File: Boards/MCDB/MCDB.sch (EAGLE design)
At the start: 61 parts, among them IC1 MC33926

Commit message: continued work on MCDB
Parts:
- added C25: 22 pF, pie:CAP0603-CAP
- added C26: 22pF, pie:CAP0603-CAP
- added C27: .1 uF, pie:CAP0603-CAP
- added C28: 1 uF, pie:CAP0603-CAP
- added R4: >VALUE, pie:R-US_R0603
- added Y1: 16MHz, pie:CRYSTAL7.6X4.1
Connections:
- new net N$17: C25.2, U$1.XTAL1, Y1.2
- new net N$18: C26.2, U$1.XTAL2, Y1.1
- new net N$19: C27.2, U$1.AREF
- new net N$21: R4.1, U$1.!RESET
- net GND: now also C25.1, C26.1, C27.1, C28.1
- net VCC: now also C28.2, R4.2
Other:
- moved on the sheet: UCAP
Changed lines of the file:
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@@
 <part name="UCAP" library="pie" deviceset="CAP" device="0603-CAP" value="1 uF"/>
 <part name="SUPPLY15" library="pie" deviceset="GND" device=""/>
+<part name="Y1" library="pie" deviceset="CRYSTAL" device="7.6X4.1" value="16MHz"/>
+<part name="C25" library="pie" deviceset="CAP" device="0603-CAP" value="22 pF"/>
+<part name="C26" library="pie" deviceset="CAP" device="0603-CAP" value="22pF"/>
+<part name="SUPPLY16" library="pie" deviceset="GND" device=""/>
+<part name="SUPPLY21" library="pie" deviceset="GND" device=""/>
+<part name="C27" library="pie" deviceset="CAP" device="0603-CAP" value=".1 uF"/>
+<part name="SUPPLY22" library="pie" deviceset="GND" device=""/>
+<part name="C28" library="pie" deviceset="CAP" device="0603-CAP" value="1 uF"/>
+<part name="SUPPLY23" library="pie" deviceset="GND" device=""/>
+<part name="R4" library="pie" deviceset="R-US_" device="R0603" value="&gt;VALUE"/>
 </parts>
 <sheets>
@@
 <attribute name="VALUE" x="157.48" y="78.74" size="1.778" layer="96"/>
 </instance>
-<instance part="UCAP" gate="G$1" x="134.62" y="121.92" smashed="yes" rot="R90">
-<attribute name="NAME" x="132.08" y="118.11" size="1.778" layer="95" rot="R90"/>
-<attribute name="VALUE" x="139.7" y="118.11" size="1.778" layer="96" rot="R90"/>
-</instance>
-<instance part="SUPPLY15" gate="GND" x="134.62" y="111.76" smashed="yes">
-<attribute name="VALUE" x="133.35" y="107.95" size="1.778" layer="96"/>
+<instance part="UCAP" gate="G$1" x="114.3" y="121.92" smashed="yes" rot="R90">
+<attribute name="NAME" x="111.76" y="118.11" size="1.778" layer="95" rot="R90"/>
+<attribute name="VALUE" x="119.38" y="118.11" size="1.778" layer="96" rot="R90"/>
+</instance>
+<instance part="SUPPLY15" gate="GND" x="114.3" y="111.76" smashed="yes">
+<attribute name="VALUE" x="113.03" y="107.95" size="1.778" layer="96"/>
+</instance>
+<instance part="Y1" gate="G$1" x="147.32" y="109.22" smashed="yes" rot="R90">
+<attribute name="NAME" x="144.78" y="109.22" size="1.778" layer="95" rot="R90"/>
+<attribute name="VALUE" x="151.13" y="106.68" size="1.778" layer="96" rot="R90"/>
+</instance>
+<instance part="C25" gate="G$1" x="129.54" y="111.76" smashed="yes">
+<attribute name="NAME" x="125.73" y="114.3" size="1.778" layer="95"/>
+<attribute name="VALUE" x="125.73" y="106.68" size="1.778" layer="96"/>
+</instance>
+<instance part="C26" gate="G$1" x="139.7" y="106.68" smashed="yes">
+<attribute name="NAME" x="135.89" y="109.22" size="1.778" layer="95"/>
+<attribute name="VALUE" x="135.89" y="101.6" size="1.778" layer="96"/>
+</instance>
+<instance part="SUPPLY16" gate="GND" x="124.46" y="104.14" smashed="yes">
+<attribute name="VALUE" x="123.19" y="100.33" size="1.778" layer="96"/>
+</instance>
+<instance part="SUPPLY21" gate="GND" x="134.62" y="99.06" smashed="yes">
+<attribute name="VALUE" x="133.35" y="95.25" size="1.778" layer="96"/>
+</instance>
+<instance part="C27" gate="G$1" x="142.24" y="139.7" smashed="yes" rot="R90">
+<attribute name="NAME" x="139.7" y="135.89" size="1.778" layer="95" rot="R90"/>
+<attribute name="VALUE" x="147.32" y="135.89" size="1.778" layer="96" rot="R90"/>
+</instance>
+<instance part="SUPPLY22" gate="GND" x="142.24" y="132.08" smashed="yes">
+<attribute name="VALUE" x="140.97" y="128.27" size="1.778" layer="96"/>
+</instance>
+<instance part="C28" gate="G$1" x="121.92" y="139.7" smashed="yes" rot="R90">
+<attribute name="NAME" x="119.38" y="135.89" size="1.778" layer="95" rot="R90"/>
+<attribute name="VALUE" x="127" y="135.89" size="1.778" layer="96" rot="R90"/>
+</instance>
+<instance part="SUPPLY23" gate="GND" x="121.92" y="132.08" smashed="yes">
+<attribute name="VALUE" x="120.65" y="128.27" size="1.778" layer="96"/>
+</instance>
+<instance part="R4" gate="G$1" x="152.4" y="167.64" smashed="yes" rot="R90">
+<attribute name="NAME" x="149.86" y="162.56" size="1.778" layer="95" rot="R90"/>
+<attribute name="VALUE" x="156.21" y="162.56" size="1.778" layer="96" rot="R90"/>
 </instance>
 </instances>
@@
 <pinref part="SUPPLY15" gate="GND" pin="GND"/>
 <pinref part="UCAP" gate="G$1" pin="1"/>
-<wire x1="134.62" y1="114.3" x2="134.62" y2="119.38" width="0.1524" layer="91"/>
+<wire x1="114.3" y1="114.3" x2="114.3" y2="119.38" width="0.1524" layer="91"/>
+</segment>
+<segment>
+<pinref part="C25" gate="G$1" pin="1"/>
+<pinref part="SUPPLY16" gate="GND" pin="GND"/>
+<wire x1="127" y1="111.76" x2="124.46" y2="111.76" width="0.1524" layer="91"/>
+<wire x1="124.46" y1="111.76" x2="124.46" y2="106.68" width="0.1524" layer="91"/>
+</segment>
+<segment>
+<pinref part="C26" gate="G$1" pin="1"/>
+<pinref part="SUPPLY21" gate="GND" pin="GND"/>
+<wire x1="137.16" y1="106.68" x2="134.62" y2="106.68" width="0.1524" layer="91"/>
+<wire x1="134.62" y1="106.68" x2="134.62" y2="101.6" width="0.1524" layer="91"/>
+</segment>
+<segment>
+<pinref part="C27" gate="G$1" pin="1"/>
+<pinref part="SUPPLY22" gate="GND" pin="GND"/>
+<wire x1="142.24" y1="137.16" x2="142.24" y2="134.62" width="0.1524" layer="91"/>
+</segment>
+<segment>
+<pinref part="C28" gate="G$1" pin="1"/>
+<pinref part="SUPPLY23" gate="GND" pin="GND"/>
+<wire x1="121.92" y1="137.16" x2="121.92" y2="134.62" width="0.1524" layer="91"/>
 </segment>
 </net>
@@
 <label x="144.78" y="132.08" size="1.778" layer="95"/>
 </segment>
+<segment>
+<pinref part="C28" gate="G$1" pin="2"/>
+<wire x1="121.92" y1="144.78" x2="121.92" y2="149.86" width="0.1524" layer="91"/>
+<label x="121.92" y="149.86" size="1.778" layer="95"/>
+</segment>
+<segment>
+<pinref part="R4" gate="G$1" pin="2"/>
+<wire x1="152.4" y1="172.72" x2="152.4" y2="175.26" width="0.1524" layer="91"/>
+<label x="152.4" y="175.26" size="1.778" layer="95"/>
+</segment>
 </net>
 <net name="PD5" class="0">
@@
 <pinref part="U$1" gate="G$1" pin="UCAP"/>
 <pinref part="UCAP" gate="G$1" pin="2"/>
-<wire x1="154.94" y1="129.54" x2="134.62" y2="129.54" width="0.1524" layer="91"/>
-<wire x1="134.62" y1="129.54" x2="134.62" y2="127" width="0.1524" layer="91"/>
-</segment>
-</net>
+<wire x1="154.94" y1="129.54" x2="114.3" y2="129.54" width="0.1524" layer="91"/>
+<wire x1="114.3" y1="129.54" x2="114.3" y2="127" width="0.1524" layer="91"/>
+</segment>
+</net>
+<net name="N$17" class="0">
+<segment>
+<pinref part="U$1" gate="G$1" pin="XTAL1"/>
+<pinref part="Y1" gate="G$1" pin="2"/>
+<wire x1="154.94" y1="111.76" x2="147.32" y2="111.76" width="0.1524" layer="91"/>
+<pinref part="C25" gate="G$1" pin="2"/>
+<wire x1="147.32" y1="111.76" x2="134.62" y2="111.76" width="0.1524" layer="91"/>
+<junction x="147.32" y="111.76"/>
+</segment>
+</net>
+<net name="N$18" class="0">
+<segment>
+<pinref part="U$1" gate="G$1" pin="XTAL2"/>
+<pinref part="Y1" gate="G$1" pin="1"/>
+<wire x1="154.94" y1="106.68" x2="147.32" y2="106.68" width="0.1524" layer="91"/>
+<pinref part="C26" gate="G$1" pin="2"/>
+<wire x1="147.32" y1="106.68" x2="144.78" y2="106.68" width="0.1524" layer="91"/>
+<junction x="147.32" y="106.68"/>
+</segment>
+</net>
+<net name="N$19" class="0">
+<segment>
+<pinref part="U$1" gate="G$1" pin="AREF"/>
+<pinref part="C27" gate="G$1" pin="2"/>
+<wire x1="154.94" y1="144.78" x2="142.24" y2="144.78" width="0.1524" layer="91"/>
+</segment>
+</net>
+<net name="N$21" class="0">
+<segment>
+<pinref part="U$1" gate="G$1" pin="!RESET"/>
+<wire x1="154.94" y1="157.48" x2="152.4" y2="157.48" width="0.1524" layer="91"/>
+<pinref part="R4" gate="G$1" pin="1"/>
+<wire x1="152.4" y1="157.48" x2="152.4" y2="162.56" width="0.1524" layer="91"/>
+</segment>
+</net>

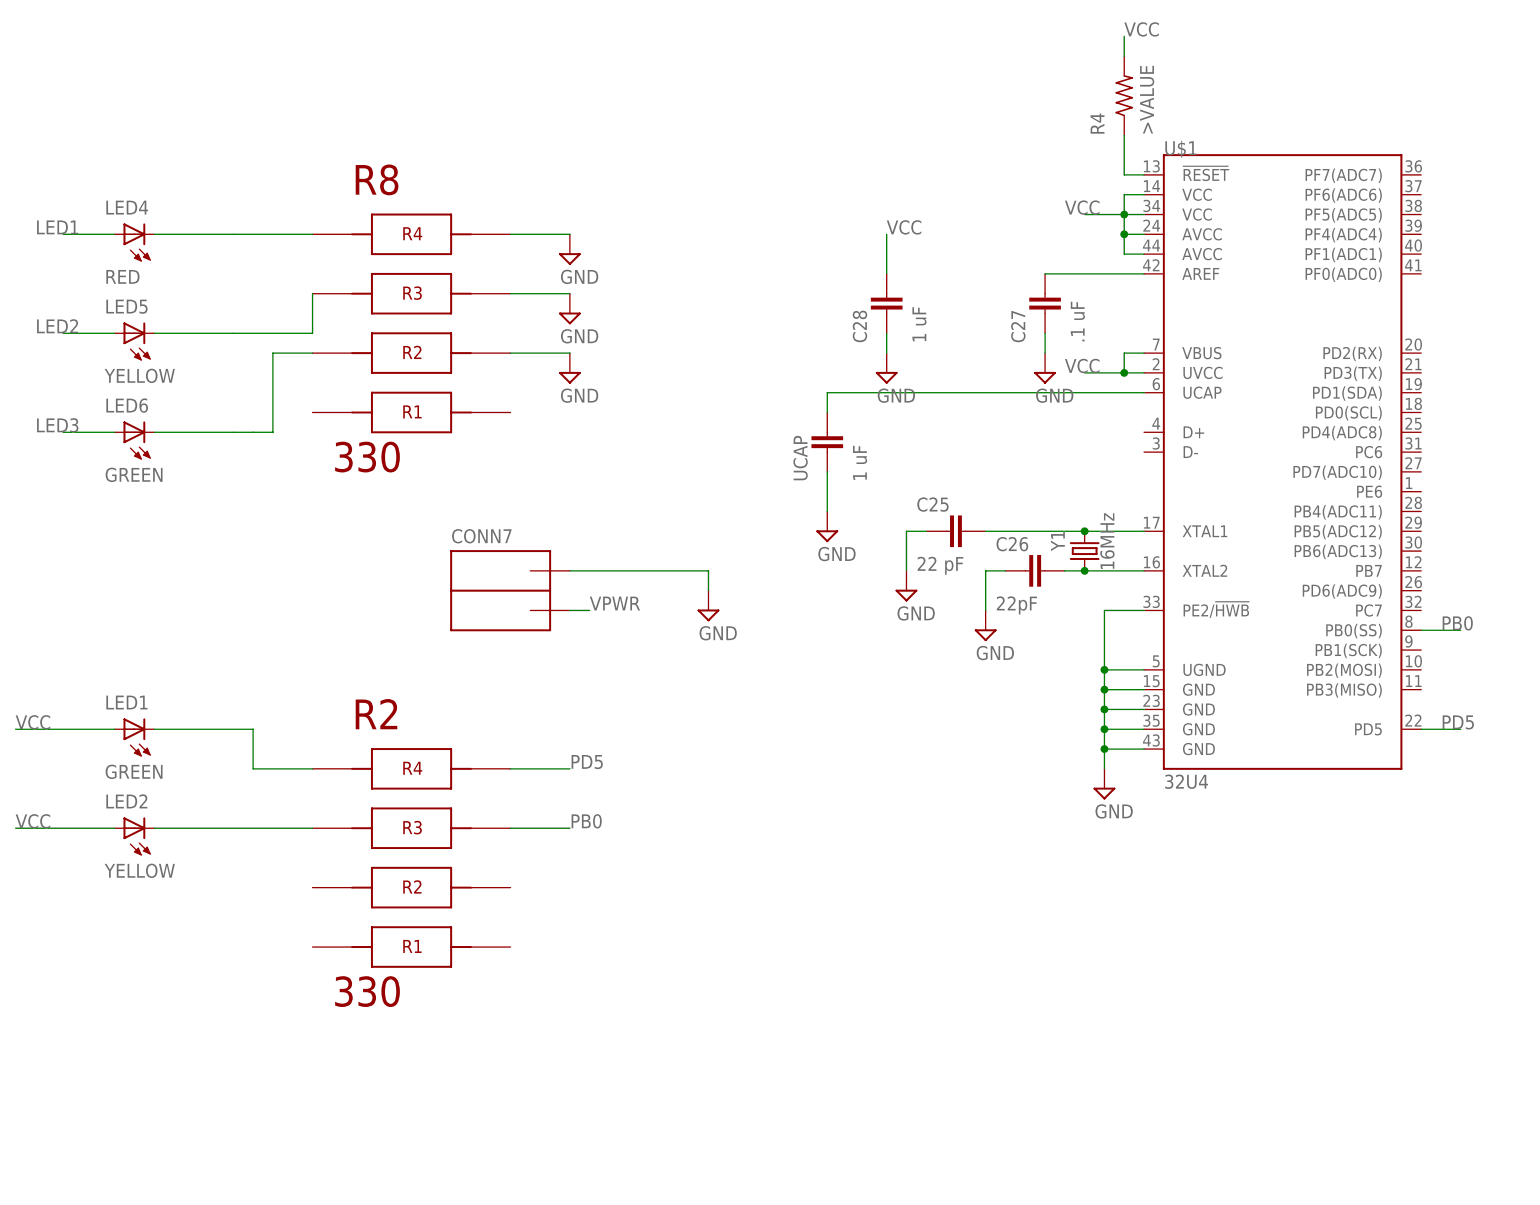
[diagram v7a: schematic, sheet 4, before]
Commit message: connected remaining pins on 32U4, added USB B and USB Micro
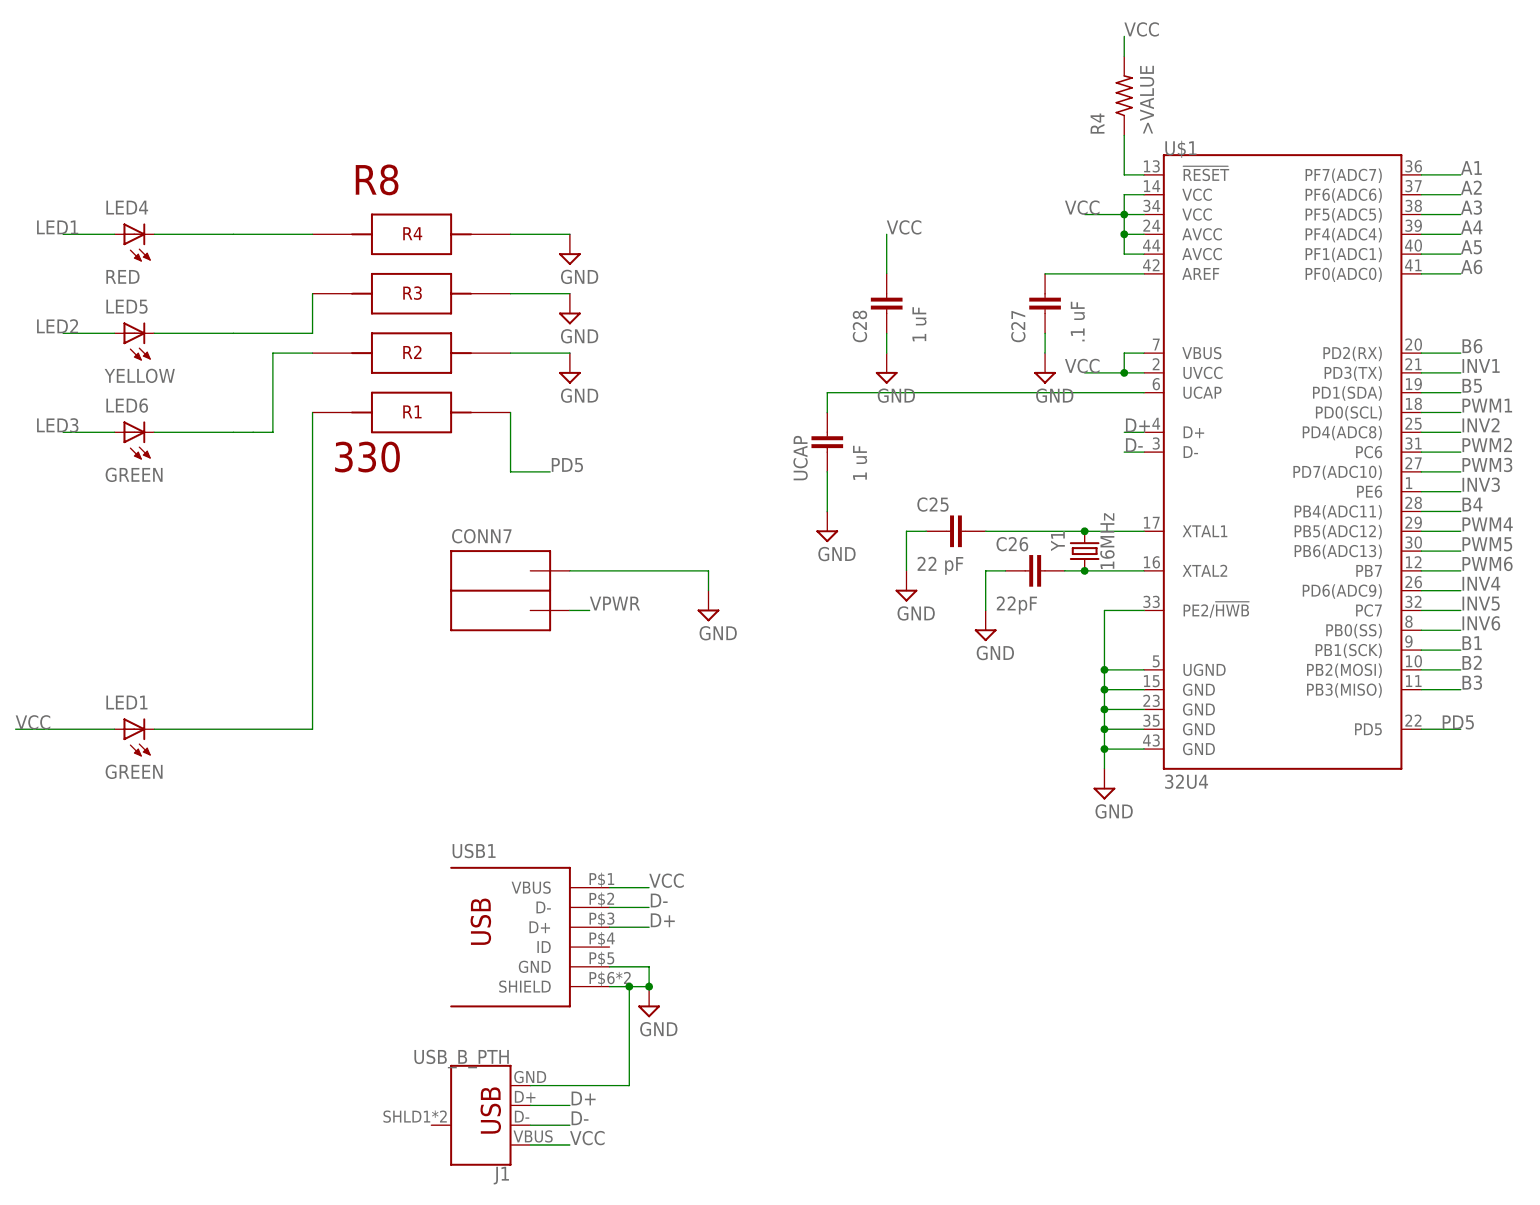
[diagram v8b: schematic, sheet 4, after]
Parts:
- removed LED2: YELLOW, pie:LED1206
- removed R2: 330, pie:4X-0603
- added J1: USB_B_PTH, SparkFun-Connectors:USB_B_PTH
- added USB1: USB-OTGMICRO-AB-VERT, pie:USB-OTGMICRO-AB-VERT
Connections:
- removed net N$13: LED2.C, R2.6
- removed net PB0: R2.3, U$1.PB0(SS)
- new net D+: J1.D+, U$1.D+, USB1.D+
- new net D-: J1.D-, U$1.D-, USB1.D-
- net A1: now also U$1.PF7(ADC7)
- net A2: now also U$1.PF6(ADC6)
- net A3: now also U$1.PF5(ADC5)
- net A4: now also U$1.PF4(ADC4)
- net A5: now also U$1.PF1(ADC1)
- net A6: now also U$1.PF0(ADC0)
- net B1: now also U$1.PB1(SCK)
- net B2: now also U$1.PB2(MOSI)
- net B3: now also U$1.PB3(MISO)
- net B4: now also U$1.PB4(ADC11)
- net B5: now also U$1.PD1(SDA)
- net B6: now also U$1.PD2(RX)
- net GND: now also J1.GND, USB1.GND, USB1.SHIELD
- net INV1: now also U$1.PD3(TX)
- net INV2: now also U$1.PD4(ADC8)
- net INV3: now also U$1.PE6
- net INV4: now also U$1.PD6(ADC9)
- net INV5: now also U$1.PC7
- net INV6: now also U$1.PB0(SS)
- net N$12: now also R8.8; no longer R2.5
- net PD5: now also R8.1; no longer R2.4
- net PWM1: now also U$1.PD0(SCL)
- net PWM2: now also U$1.PC6
- net PWM3: now also U$1.PD7(ADC10)
- net PWM4: now also U$1.PB5(ADC12)
- net PWM5: now also U$1.PB6(ADC13)
- net PWM6: now also U$1.PB7
- net VCC: now also J1.VBUS, USB1.VBUS; no longer LED2.A
